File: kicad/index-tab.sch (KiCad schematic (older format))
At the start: 25 parts, among them J1 USB_C_Receptacle_USB2.0, SW1 SW_Push, U1 ATmega32U4-MU, U2 MIC5219-5.0YM5, Y1 16MHz

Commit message: Switched to 0603 and redrawn the PCB
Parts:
- removed C9: 100nF, Capacitor_SMD:C_1206_3216Metric_Pad1.42x1.75mm_HandSolder, symbol Device:C
- removed D101: PRTR5V0U2X, Package_TO_SOT_SMD:SOT-143, symbol Power_Protection:PRTR5V0U2X
- removed D102: D, Diode_SMD:D_1206_3216Metric_Pad1.42x1.75mm_HandSolder, symbol Device:D
- removed U2: MIC5219-5.0YM5, Package_TO_SOT_SMD:SOT-23-5_HandSoldering, symbol Regulator_Linear:MIC5219-5.0YM5
- added D102: 3A/10V/280mV, Diode_SMD:D_SOD-323_HandSoldering, symbol Device:D_Schottky
- C1, C2, C4: footprint Capacitor_SMD:C_1206_3216Metric_Pad1.42x1.75mm_HandSolder -> Capacitor_SMD:C_0603_1608Metric_Pad1.05x0.95mm_HandSolder
- C3: value 100nF -> 0.1uF; footprint Capacitor_SMD:C_1206_3216Metric_Pad1.42x1.75mm_HandSolder -> Capacitor_SMD:C_0603_1608Metric_Pad1.05x0.95mm_HandSolder
- C5: value 1uF -> 10uF; footprint Capacitor_SMD:C_1206_3216Metric_Pad1.42x1.75mm_HandSolder -> Capacitor_SMD:C_0603_1608Metric_Pad1.05x0.95mm_HandSolder
- C6, C7: value 10uF -> 1uF; footprint Capacitor_SMD:C_1206_3216Metric_Pad1.42x1.75mm_HandSolder -> Capacitor_SMD:C_0603_1608Metric_Pad1.05x0.95mm_HandSolder
- C8: value 1uF -> 0.1uF; footprint Capacitor_SMD:C_1206_3216Metric_Pad1.42x1.75mm_HandSolder -> Capacitor_SMD:C_0603_1608Metric_Pad1.05x0.95mm_HandSolder
- F1: value 500mA -> 6v 0.5A
- LED1: renamed from D103; footprint LED_SMD:LED_1206_3216Metric_Pad1.42x1.75mm_HandSolder -> LED_SMD:LED_0603_1608Metric_Pad1.05x0.95mm_HandSolder
- R1, R2, R3, R4, R5, R6, R7: footprint Resistor_SMD:R_1206_3216Metric_Pad1.42x1.75mm_HandSolder -> Resistor_SMD:R_0603_1608Metric_Pad1.05x0.95mm_HandSolder
- U1: value ATmega32U4-MU -> ATmega32U4-AU; footprint Package_DFN_QFN:QFN-44-1EP_7x7mm_P0.5mm_EP5.2x5.2mm -> Package_QFP:TQFP-44_10x10mm_P0.8mm; symbol MCU_Microchip_ATmega:ATmega32U4-MU -> MCU_Microchip_ATmega:ATmega32U4-AU
- Y1: footprint Crystal:Crystal_SMD_3225-4Pin_3.2x2.5mm_HandSoldering -> Crystal:Crystal_SMD_0603-4Pin_6.0x3.5mm
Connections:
- net labels added: +5v, AREF, D+, D-, RESET, UCAP, V_USB
- net labels removed: UVCC, VCC
- wire segments 124 -> 92
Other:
- moved on the sheet: C1, C2, C3, C4, J1, LED1, R1, R2, R3, R4, R5, R6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

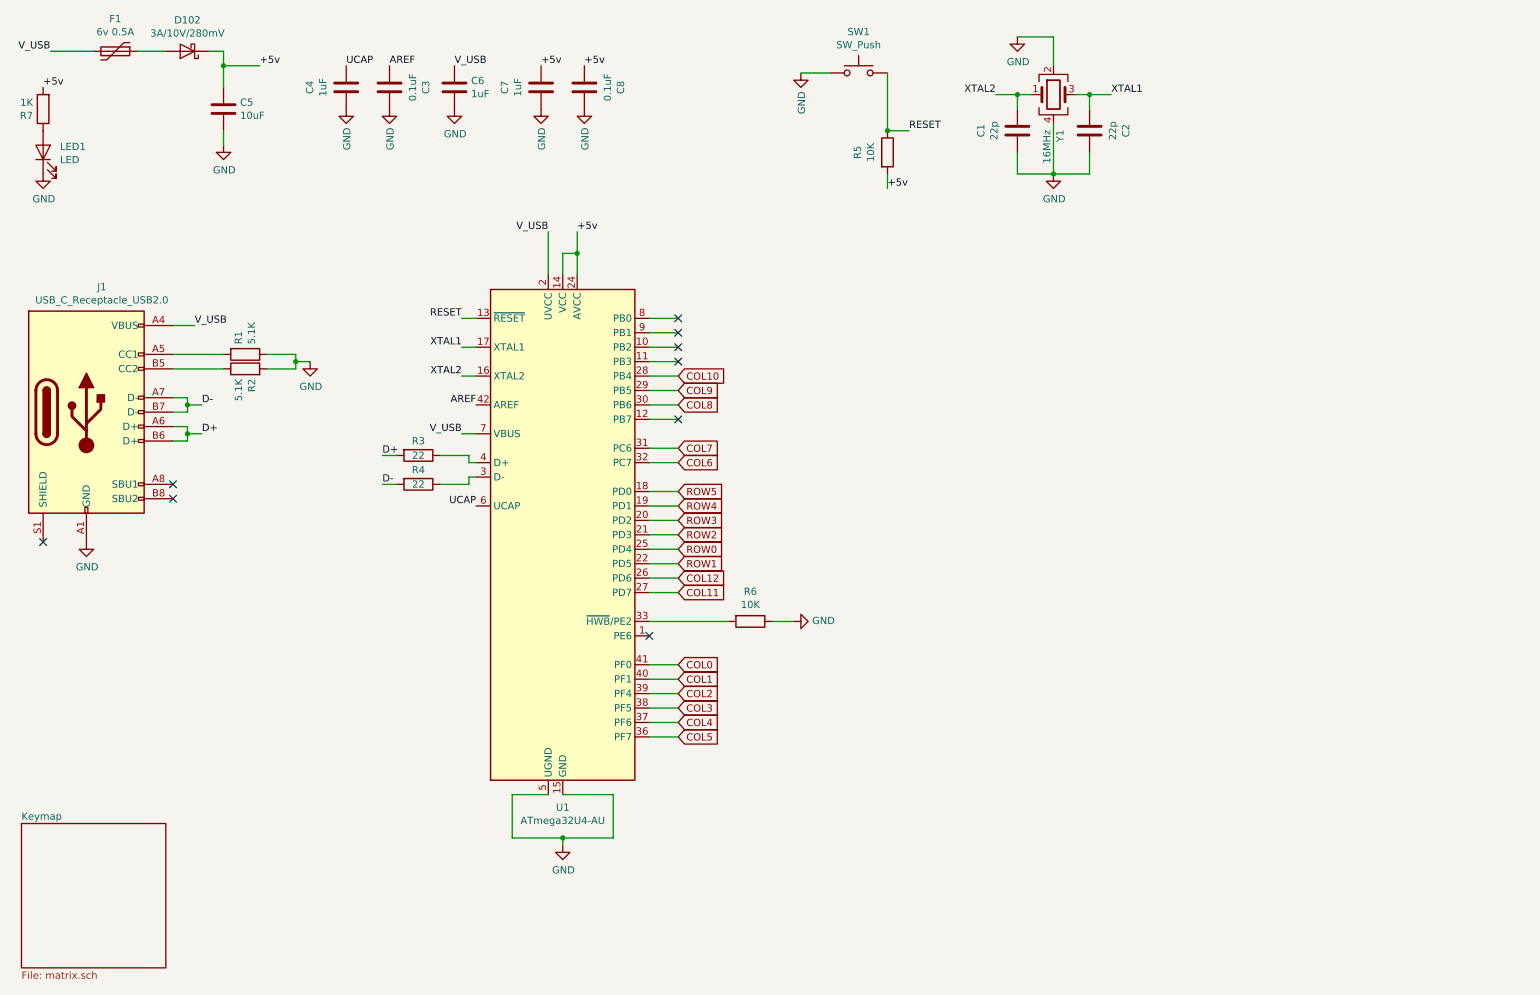
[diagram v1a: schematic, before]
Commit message: Added RGB and a monster to the f.silk
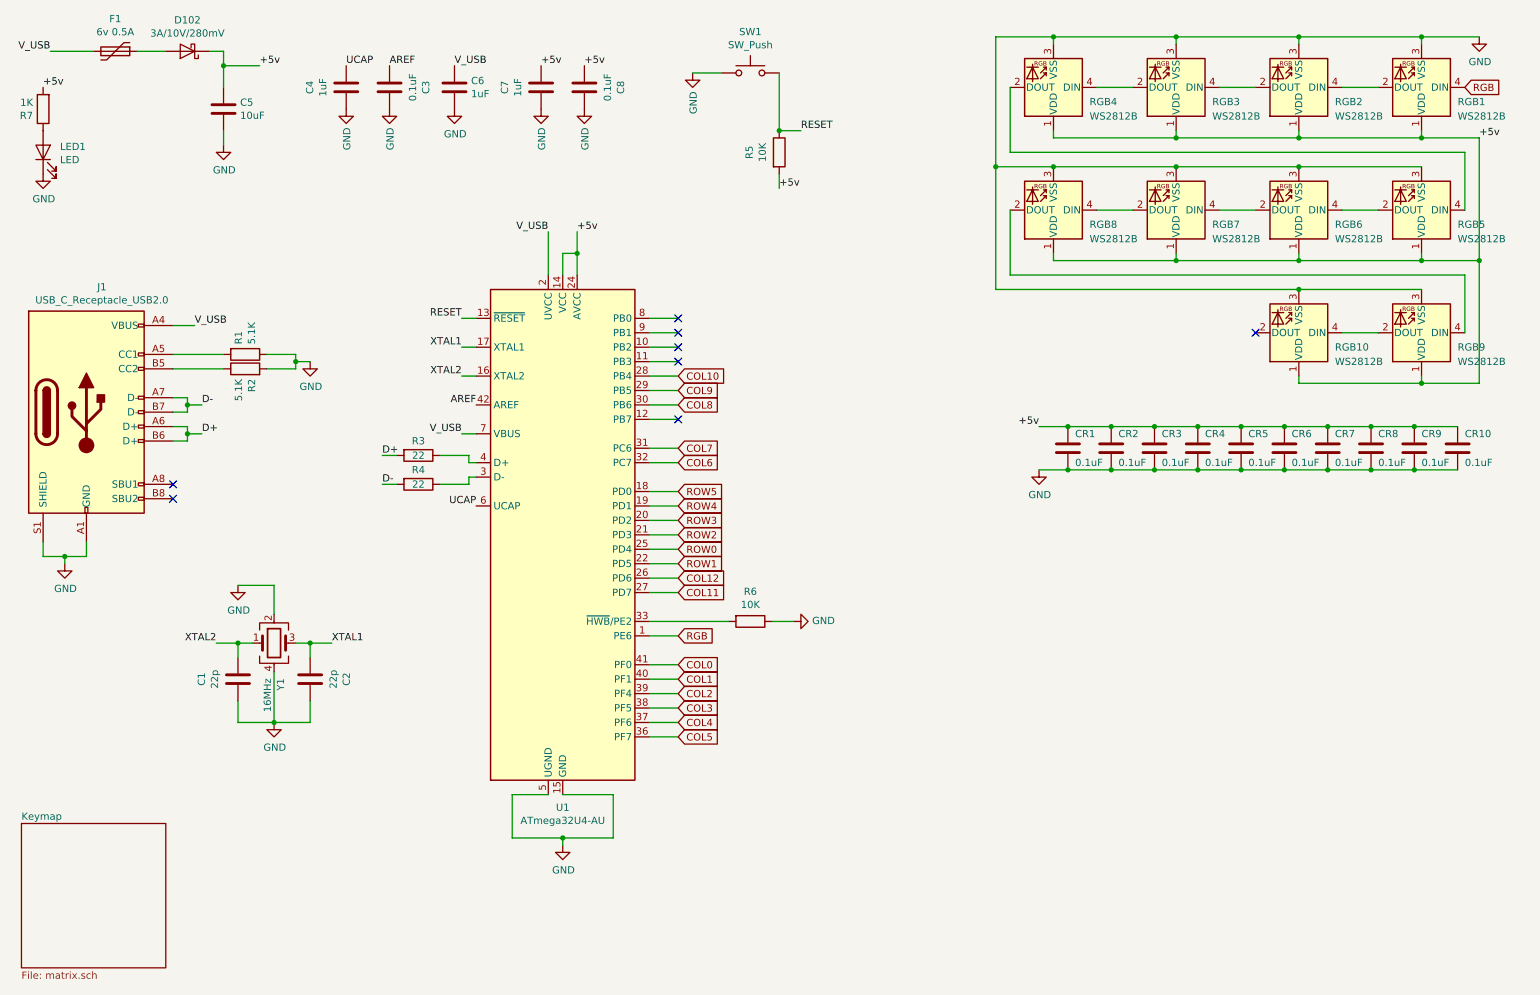
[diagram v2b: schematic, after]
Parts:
- added CR1, CR10, CR2, CR3, CR4, CR5, CR6, CR7, CR8, CR9: 0.1uF, Capacitor_SMD:C_0603_1608Metric_Pad1.05x0.95mm_HandSolder, symbol Device:C
- added RGB1, RGB10, RGB2, RGB3, RGB4, RGB5, RGB6, RGB7, RGB8, RGB9: WS2812B, LED_SMD:LED_WS2812B_PLCC4_5.0x5.0mm_P3.2mm, symbol LED:WS2812B
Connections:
- net +5v: now also CR1.1, CR10.1, CR2.1, CR3.1, CR4.1, CR5.1, CR6.1, CR7.1, CR8.1, CR9.1, RGB1.1 (VDD), RGB10.1 (VDD), RGB2.1 (VDD), RGB3.1 (VDD), RGB4.1 (VDD), RGB5.1 (VDD), RGB6.1 (VDD), RGB7.1 (VDD), RGB8.1 (VDD), RGB9.1 (VDD)
- net GND: now also J1.S1 (SHIELD), CR1.2, CR10.2, CR2.2, CR3.2, CR4.2, CR5.2, CR6.2, CR7.2, CR8.2, CR9.2, RGB1.3 (VSS), RGB10.3 (VSS), RGB2.3 (VSS), RGB3.3 (VSS), RGB4.3 (VSS), RGB5.3 (VSS), RGB6.3 (VSS), RGB7.3 (VSS), RGB8.3 (VSS), RGB9.3 (VSS)
- net RGB: now reaches U1.1 (PE6)
- net RGB: now also RGB1.4 (DIN)
- new net: RGB1.2 (DOUT), RGB2.4 (DIN)
- new net: RGB4.2 (DOUT), RGB5.4 (DIN)
- new net: RGB3.2 (DOUT), RGB4.4 (DIN)
- new net: RGB2.2 (DOUT), RGB3.4 (DIN)
- new net: RGB5.2 (DOUT), RGB6.4 (DIN)
- new net: RGB6.2 (DOUT), RGB7.4 (DIN)
- new net: RGB7.2 (DOUT), RGB8.4 (DIN)
- new net: RGB8.2 (DOUT), RGB9.4 (DIN)
- new net: RGB10.4 (DIN), RGB9.2 (DOUT)
- no-connect marks 9 -> 8
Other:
- moved on the sheet: C1, C2, R5, SW1, Y1

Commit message: Retraced and rebuild the PCB
Fixed wrong footprint for diodes and crystal. Trying out a new USB-C, but probably changing back before order of rev2. Also added ESD for safty.
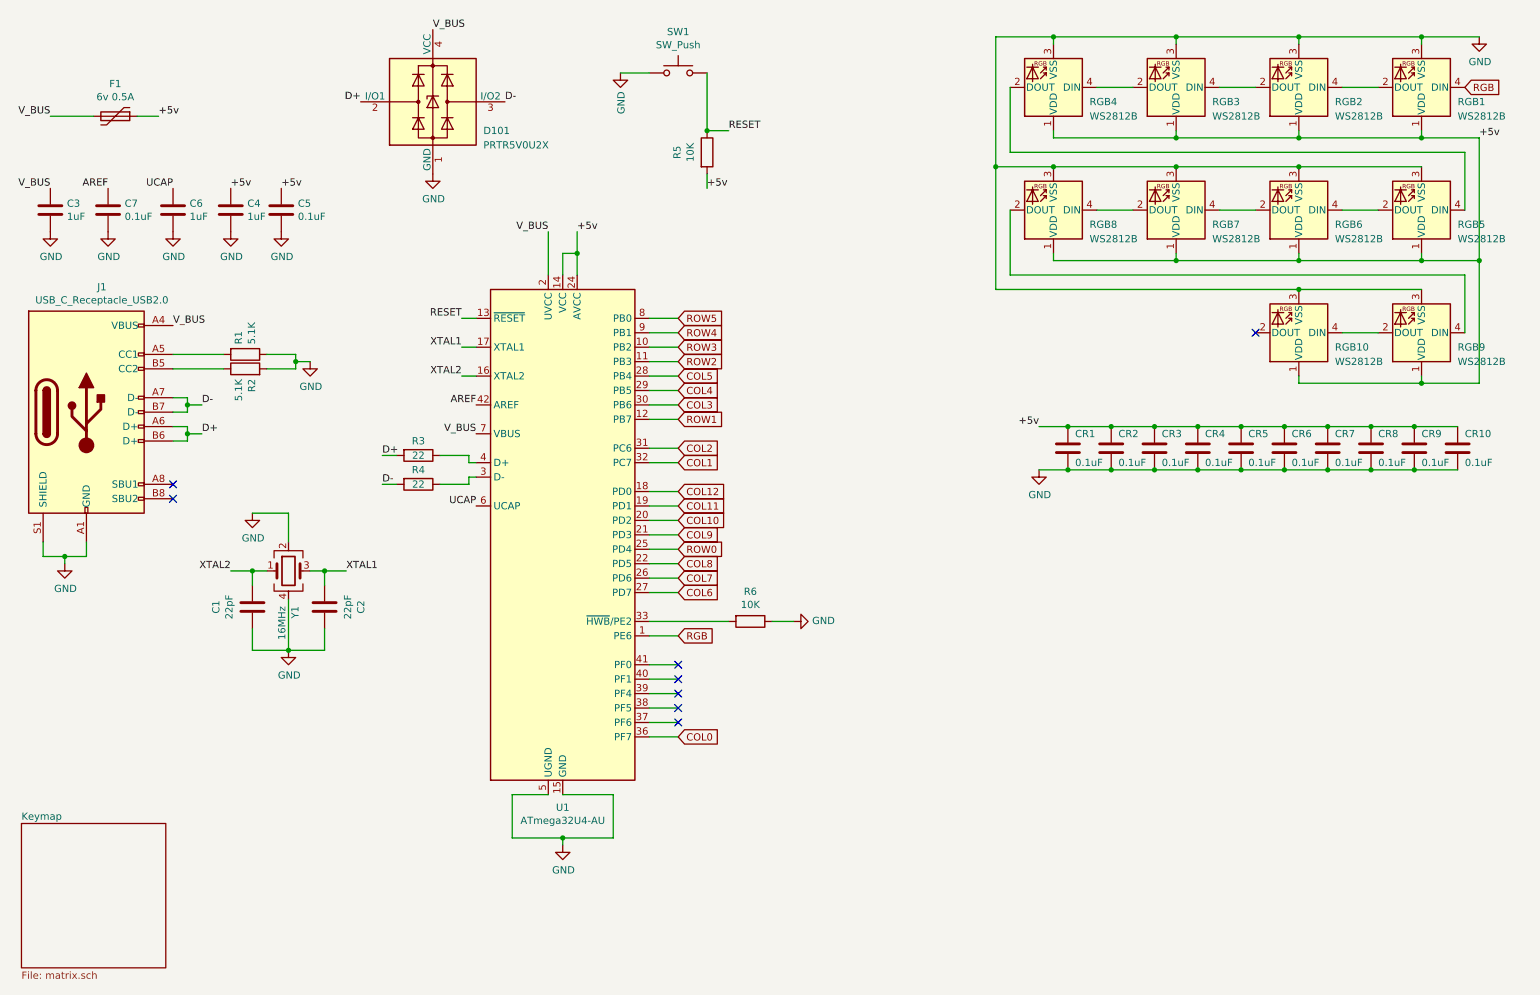
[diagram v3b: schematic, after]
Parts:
- removed C8: 0.1uF, Capacitor_SMD:C_0603_1608Metric_Pad1.05x0.95mm_HandSolder, symbol Device:C
- removed D102: 3A/10V/280mV, Diode_SMD:D_SOD-323_HandSoldering, symbol Device:D_Schottky
- removed LED1: LED, LED_SMD:LED_0603_1608Metric_Pad1.05x0.95mm_HandSolder, symbol Device:LED
- removed R7: 1K, Resistor_SMD:R_0603_1608Metric_Pad1.05x0.95mm_HandSolder, symbol Device:R
- added D101: PRTR5V0U2X, Package_TO_SOT_SMD:SOT-143, symbol Power_Protection:PRTR5V0U2X
- C1, C2: value 22p -> 22pF
- C3: value 0.1uF -> 1uF
- C5: value 10uF -> 0.1uF
- C7: value 1uF -> 0.1uF
- J1: footprint Connector_USB:USB_C_Receptacle_HRO_TYPE-C-31-M-12 -> Connector_USB:USB_C_Receptacle_GCT_USB4085
- Y1: footprint Crystal:Crystal_SMD_0603-4Pin_6.0x3.5mm -> Crystal:Crystal_SMD_3225-4Pin_3.2x2.5mm_HandSoldering
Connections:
- net +5v: now also C4.1, F1.1; no longer C7.1
- net AREF: now also C7.1; no longer C3.1
- net COL0: now also U1.36 (PF7); no longer U1.41 (PF0)
- net COL1: now also U1.32 (PC7); no longer U1.40 (PF1)
- net COL10: now also U1.20 (PD2); no longer U1.28 (PB4)
- net COL11: now also U1.19 (PD1); no longer U1.27 (PD7)
- net COL12: now also U1.18 (PD0); no longer U1.26 (PD6)
- net COL2: now also U1.31 (PC6); no longer U1.39 (PF4)
- net COL3: now also U1.30 (PB6); no longer U1.38 (PF5)
- net COL4: now also U1.29 (PB5); no longer U1.37 (PF6)
- net COL5: now also U1.28 (PB4); no longer U1.36 (PF7)
- net COL6: now also U1.27 (PD7); no longer U1.32 (PC7)
- net COL7: now also U1.26 (PD6); no longer U1.31 (PC6)
- net COL8: now also U1.22 (PD5); no longer U1.30 (PB6)
- net COL9: now also U1.21 (PD3); no longer U1.29 (PB5)
- net D+: now also D101.2 (I/O1)
- net D-: now also D101.3 (I/O2)
- net GND: now also D101.1 (GND)
- net ROW1: now also U1.12 (PB7); no longer U1.22 (PD5)
- net ROW2: now also U1.11 (PB3); no longer U1.21 (PD3)
- net ROW3: now also U1.10 (PB2); no longer U1.20 (PD2)
- net ROW4: now also U1.9 (PB1); no longer U1.19 (PD1)
- net ROW5: now also U1.8 (PB0); no longer U1.18 (PD0)
- net UCAP: now also C6.1; no longer C4.1
- net V_USB renamed V_BUS
- net V_BUS: now also C3.1, D101.4 (VCC); no longer C6.1
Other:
- moved on the sheet: C1, C2, F1, R5, SW1, Y1

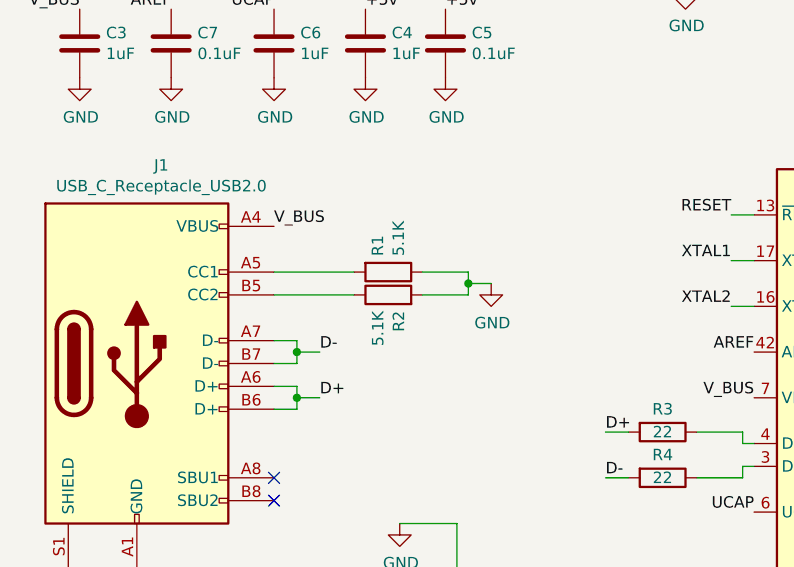
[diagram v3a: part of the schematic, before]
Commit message: Changed USB-C and added more gnd
Suing the easier HRO TYPE-C-31-M-12
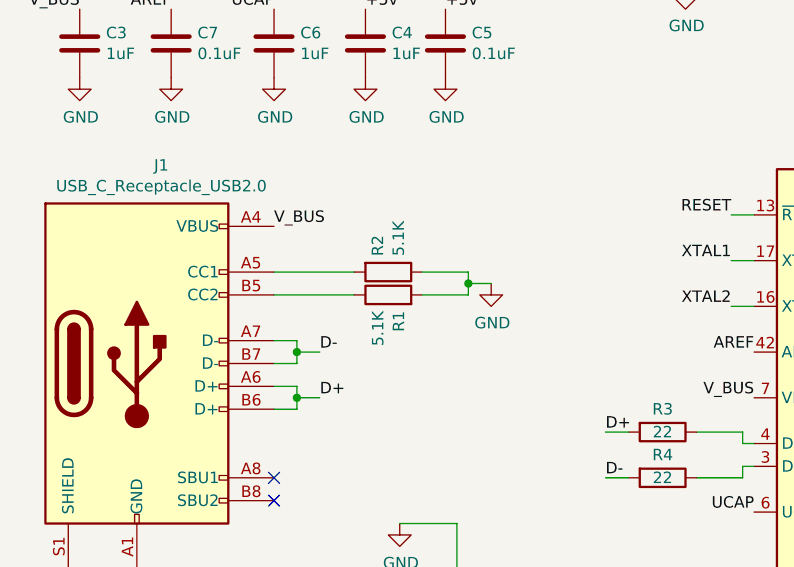
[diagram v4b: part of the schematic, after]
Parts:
- J1: footprint Connector_USB:USB_C_Receptacle_GCT_USB4085 -> Connector_USB:USB_C_Receptacle_HRO_TYPE-C-31-M-12
- renumbered R2 to R1, R1 to R2
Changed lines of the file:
@@
 F 0 "J1" H 1307 4267 50  0000 C CNN
 F 1 "USB_C_Receptacle_USB2.0" H 1307 4176 50  0000 C CNN
-F 2 "Connector_USB:USB_C_Receptacle_GCT_USB4085" H 1350 3400 50  0001 C CNN
+F 2 "Connector_USB:USB_C_Receptacle_HRO_TYPE-C-31-M-12" H 1350 3400 50  0001 C CNN
 F 3 "https://www.usb.org/sites/default/files/documents/usb_type-c.zip" H 1350 3400 50  0001 C CNN
 	1    1200 3400
@@
 	2450 3100 2650 3100
 $Comp
-L Device:R R1
+L Device:R R2
 U 1 1 5E4988A3
 P 2300 3000
-F 0 "R1" H 2230 2954 50  0000 R CNN
+F 0 "R2" H 2230 2954 50  0000 R CNN
 F 1 "5.1K" H 2230 3045 50  0000 R CNN
 F 2 "Resistor_SMD:R_0603_1608Metric_Pad1.05x0.95mm_HandSolder" V 2230 3000 50  0001 C CNN
@@
 $EndComp
 $Comp
-L Device:R R2
+L Device:R R1
 U 1 1 5E496DB2
 P 2300 3100
-F 0 "R2" H 2230 3054 50  0000 R CNN
+F 0 "R1" H 2230 3054 50  0000 R CNN
 F 1 "5.1K" H 2230 3145 50  0000 R CNN
 F 2 "Resistor_SMD:R_0603_1608Metric_Pad1.05x0.95mm_HandSolder" V 2230 3100 50  0001 C CNN

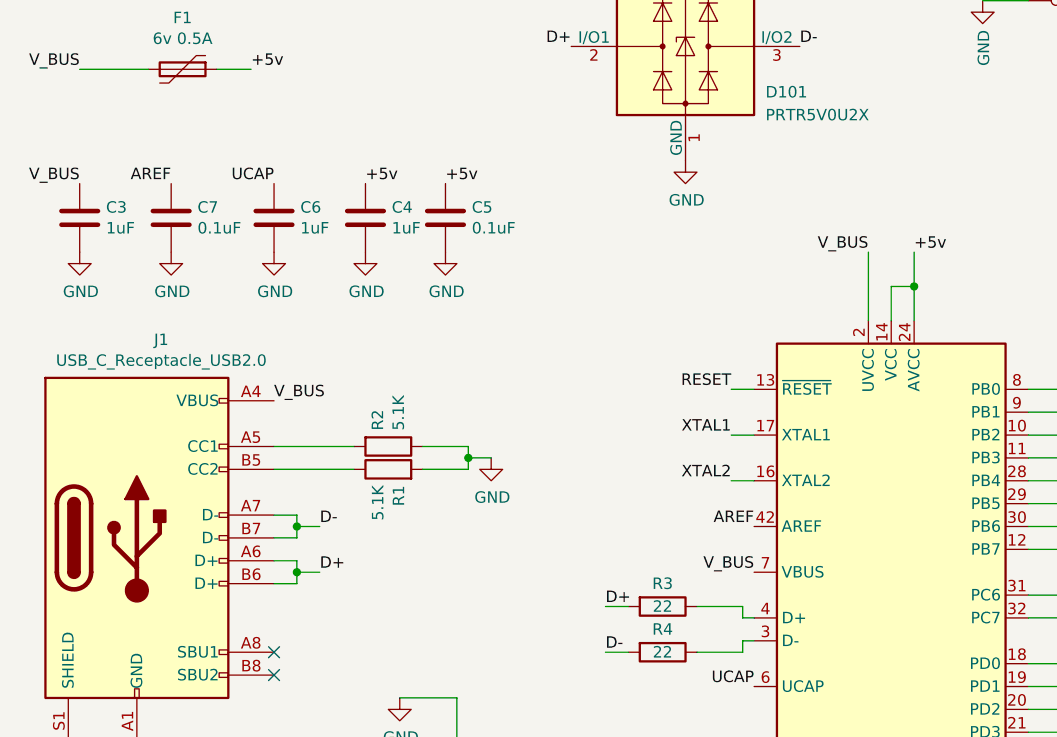
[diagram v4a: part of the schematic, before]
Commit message: rev2 ordered
this was done before I've managed to get rev1 working. Post coming about it. rev2 looks more like UT47.2
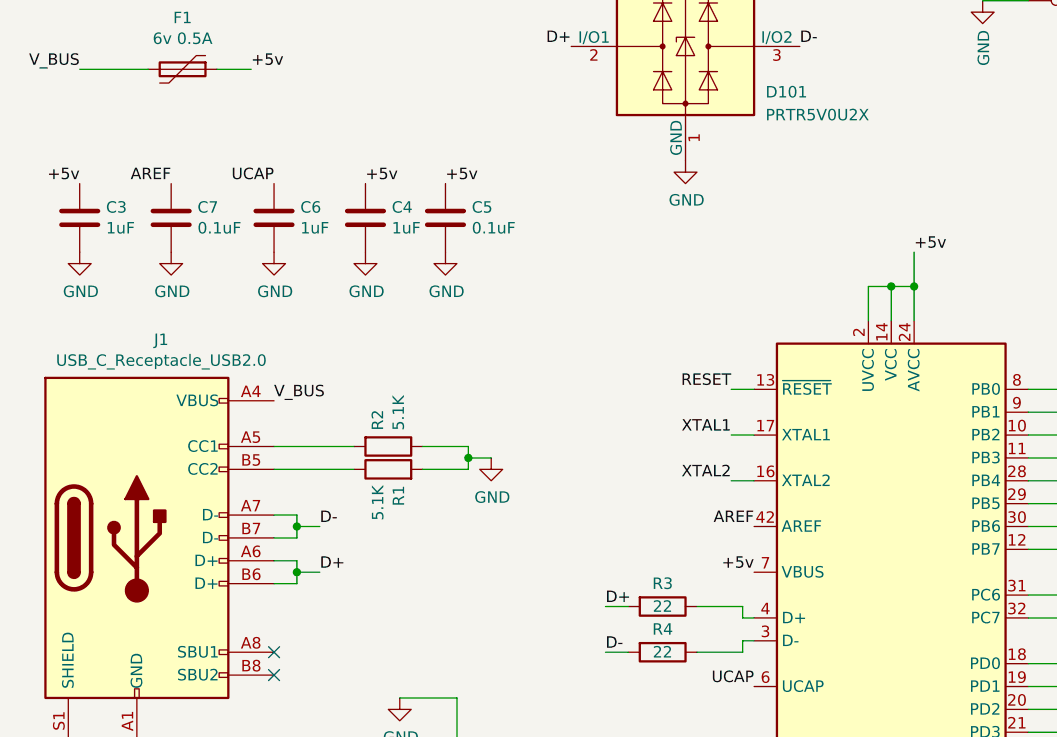
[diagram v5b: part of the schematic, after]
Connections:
- net +5v: now also C3.1, U1.2 (UVCC), U1.7 (VBUS)
- net V_BUS: no longer C3.1, U1.2 (UVCC), U1.7 (VBUS)
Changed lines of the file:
@@
 V_BUS
 Text Label 3900 3550 2    50   ~ 0
-V_BUS
-Text Label 4400 2150 2    50   ~ 0
-V_BUS
++5v
 Wire Wire Line
-	4400 2150 4400 2450
+	4400 2300 4400 2450
 Text Label 950  1350 2    50   ~ 0
 V_BUS
 Text Label 950  1850 2    50   ~ 0
-V_BUS
++5v
 $Comp
 L Device:C C3
@@
 Text GLabel 5300 5650 2    50   Input ~ 0
 COL0
+Wire Wire Line
+	4400 2300 4500 2300
+Connection ~ 4500 2300
 $EndSCHEMATC
